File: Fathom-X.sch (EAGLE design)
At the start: 33 parts

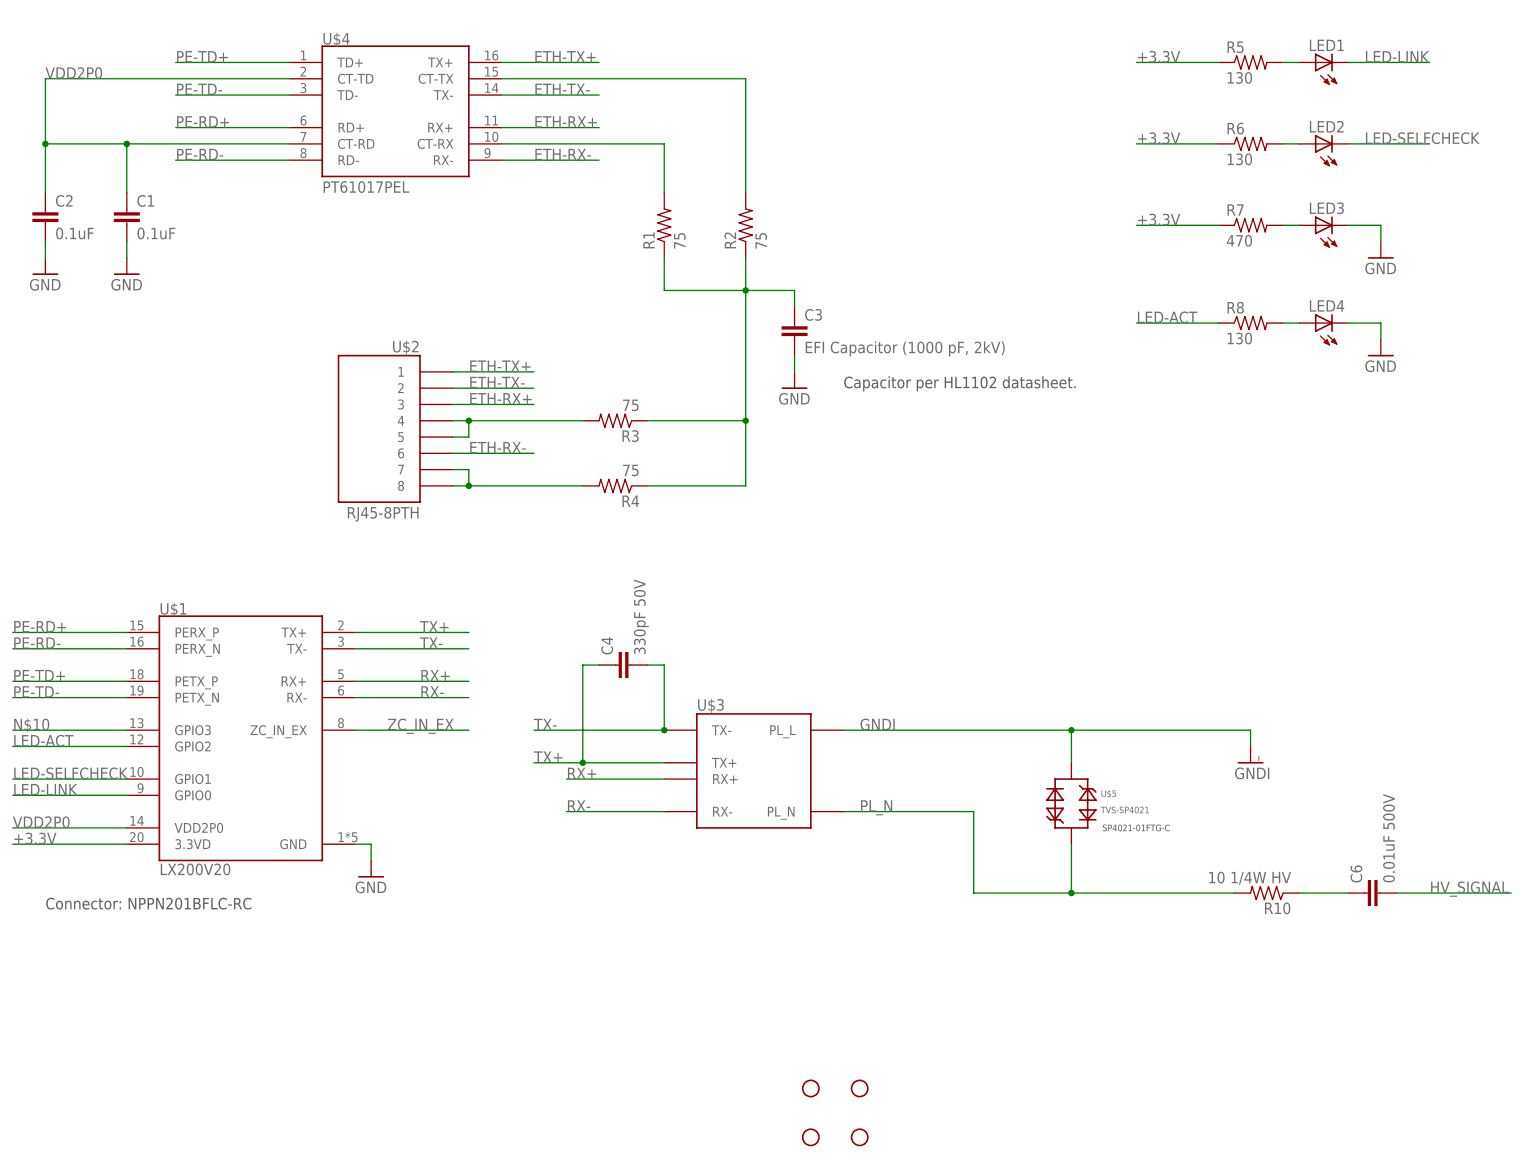
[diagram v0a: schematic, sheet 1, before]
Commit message: Divide to Fathom-E and Fathom-X. Both boards of this revision were ordered.
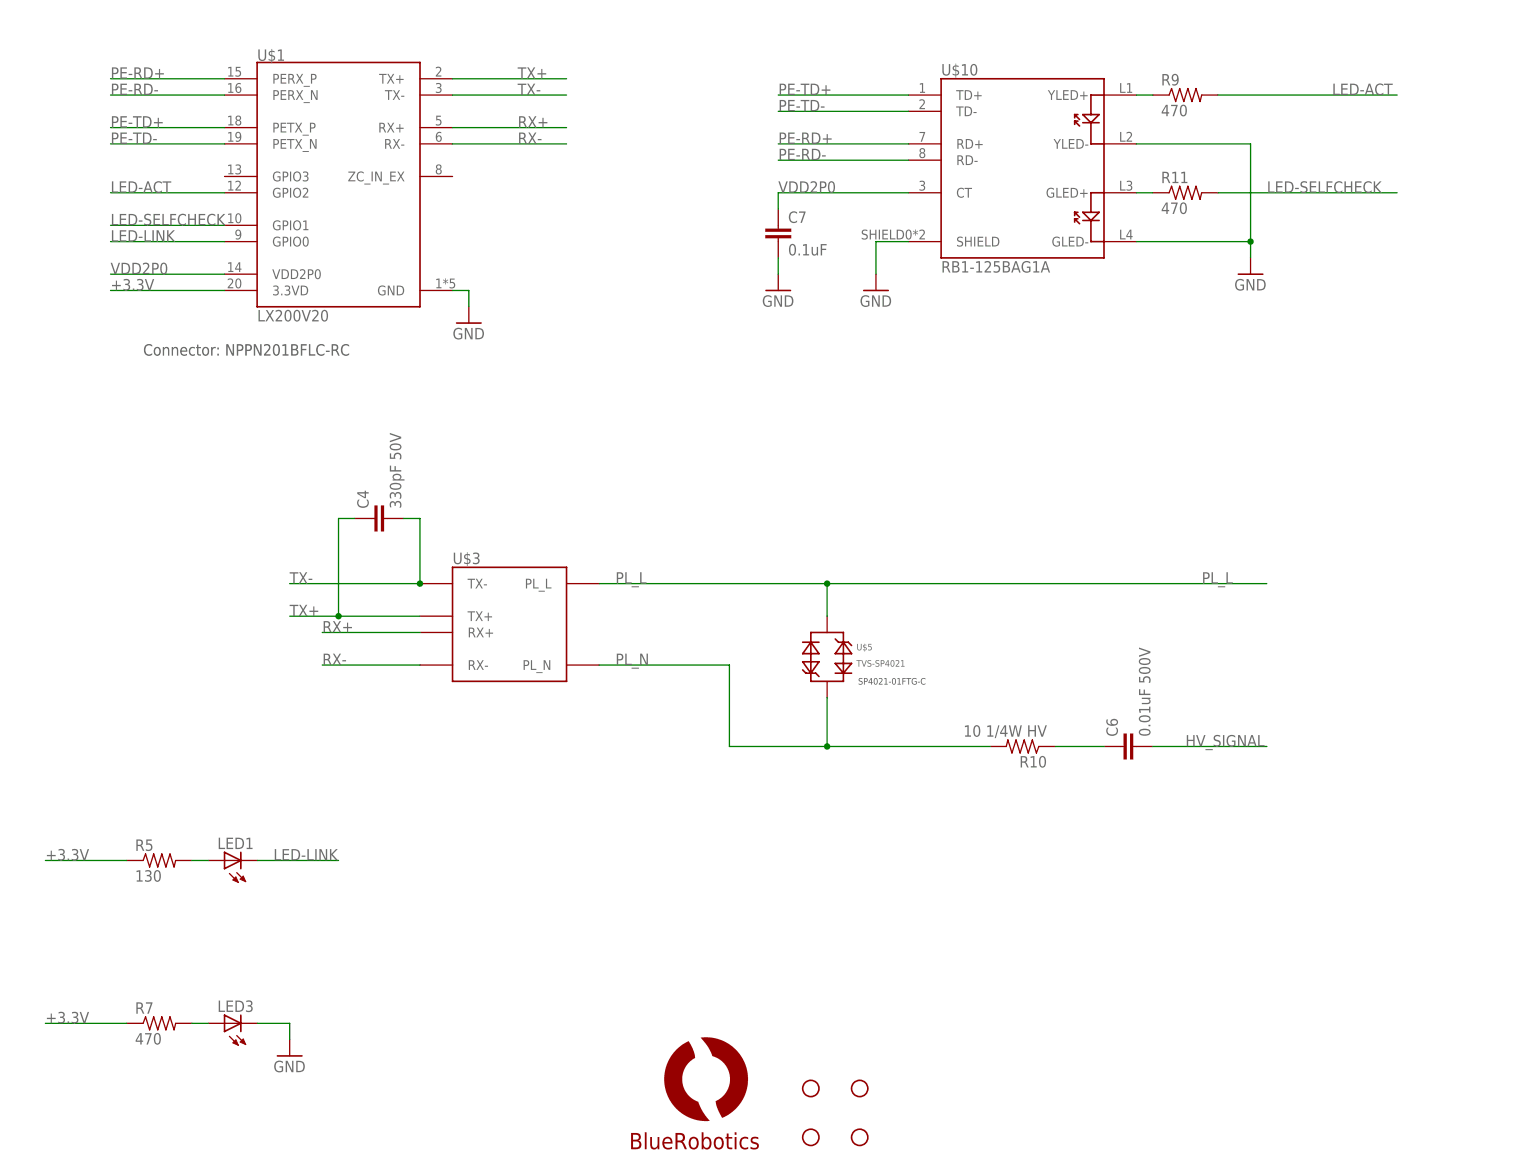
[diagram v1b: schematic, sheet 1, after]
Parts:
- removed C2: 0.1uF, resistor:C-EUC0402
- removed C3: EFI Capacitor (1000 pF, 2kV), resistor:C-EUC1206
- removed C5: 10uF, resistor:C-USC1206
- removed LED2, LED4: (no value), led:LEDCHIPLED_0603
- removed R1, R2, R3, R4: 75, resistor:R-US_R0603
- removed R6, R8: 130, resistor:R-US_R0603
- removed U$8: HEADER-2POWER, BlueRobotics-Main:HEADER-2POWER
- added C15: 0.1uF, SparkFun-Passives:CAP0603-CAP
- added C16: 10uF 10V, SparkFun-Passives:CAP_POL1206
- added C7: 0.1uF, resistor:C-EUC0603
- added D1: B340A, SparkFun-DiscreteSemi:DIODE-SCHOTTKY-B340A
- added IC1: 1117-3.3V, BlueRobotics-Main:VREG-1117-FIXEDSOT223
- added JP2: M023.5MM, SparkFun-Connectors:M023.5MM
- added JP3: USBSMD, SparkFun-Connectors:USBSMD
- added R11, R9: 470, resistor:R-US_R0603
- added U$10: RB1-125BAG1A, BlueRobotics-Main:RJ45-MAG
- C1: value 0.1uF -> 10uF 10V; device resistor:C-EUC0402 -> SparkFun-Passives:CAP_POL1206
- JP1: value (none) -> M02PTH; device SparkFun-Connectors:M083.5MM-8 -> SparkFun-Connectors:M02PTH
- U$2: value RJ45-8PTH -> HEADER-1NQ; device BlueRobotics-Main:RJ45-8PTH -> BlueRobotics-Main:HEADER-1NQ
- U$4: value PT61017PEL -> HEADER-1NQ; device BlueRobotics-Main:PT61017PEL -> BlueRobotics-Main:HEADER-1NQ
- U$6: value TETHER-HEADERSERIAL -> LOGOBR-LOGO-MS-COPPER; device BlueRobotics-Main:TETHER-HEADERSERIAL -> BlueRobotics-Main:LOGOBR-LOGO-MS-COPPER
- U$7: value HEADER-2POWER -> LOGOFULL-M; device BlueRobotics-Main:HEADER-2POWER -> BlueRobotics-Main:LOGOFULL-M
- U$9: value OKI-78SR-3.3V -> R-78E-0.5; device BlueRobotics-Main:VREG-OKI-78SR -> BlueRobotics-Main:VREG-R-78E-0.5
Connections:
- removed net 3.3V: C5.1, U$9.OUT
- removed net ETH-RX+: U$2.3, U$4.RX+
- removed net ETH-RX-: U$2.6, U$4.RX-
- removed net ETH-TX+: U$2.1, U$4.TX+
- removed net ETH-TX-: U$2.2, U$4.TX-
- removed net GNDI: JP1.3, U$3.PL_L, U$5.P$2
- removed net N$10: U$1.GPIO3
- removed net N$2: R2.2, U$4.CT-TX
- removed net N$3: R4.2, U$2.7, U$2.8
- removed net N$4: C3.1, R1.1, R2.1, R3.1, R4.1
- removed net N$5: R3.2, U$2.4, U$2.5
- removed net N$7: LED2.A, R6.2
- removed net N$9: LED4.A, R8.2
- removed net ZC_IN_EX: U$1.ZC_IN_EX
- new net 5V: C1.+, C15.1, D1.C, IC1.IN, U$9.OUT
- new net N$12: R9.1, U$10.YLED+
- new net N$13: R11.1, U$10.GLED+
- new net PL_L: JP1.2, U$3.PL_L, U$4.1, U$5.P$2
- net +3.3V: now also C16.+, IC1.OUT; no longer R6.1
- net GND: now also C1.-, C15.2, C16.-, C7.2, IC1.GND, JP2.1, JP3.GND, U$10.GLED-, U$10.SHIELD, U$10.YLED-; no longer C1.2, C2.2, C3.2, C5.2, LED4.C, U$7.1
- net HV_SIGNAL: now also U$2.1; no longer JP1.4
- net LED-ACT: now also R9.2; no longer R8.1
- net LED-SELFCHECK: now also R11.2; no longer LED2.C
- net N$1: now also D1.A, JP3.VBUS; no longer R1.2, U$4.CT-RX
- net PE-RD+: now also U$10.RD+; no longer U$4.RD+
- net PE-RD-: now also U$10.RD-; no longer U$4.RD-
- net PE-TD+: now also U$10.TD+; no longer U$4.TD+
- net PE-TD-: now also U$10.TD-; no longer U$4.TD-
- net PL_N: now also JP1.1
- net VDD2P0: now also C7.1, U$10.CT; no longer C1.1, C2.1, U$4.CT-RD, U$4.CT-TD
- net VIN: now also JP2.2; no longer U$7.2
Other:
- note removed: "Capacitor per HL1102 datasheet."
- moved on the sheet: C4, C6, LED1, LED3, R10, R5, R7, U$1, U$3, U$5, U$9

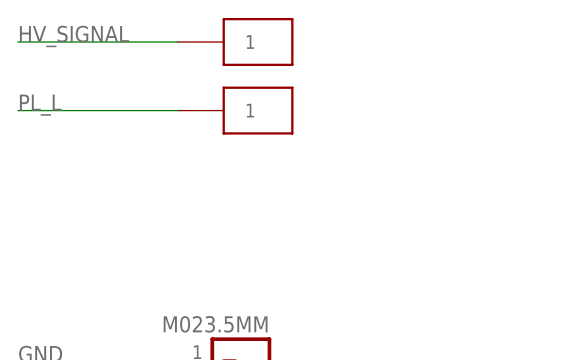
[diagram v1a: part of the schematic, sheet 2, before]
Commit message: Fathom-X: Update signal connector
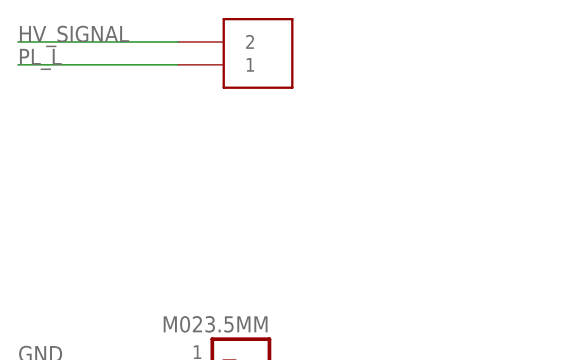
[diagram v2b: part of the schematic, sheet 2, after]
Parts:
- removed U$2, U$4: HEADER-1NQ, BlueRobotics-Main:HEADER-1NQ
- added U$8: HEADER-2POWER, BlueRobotics-Main:HEADER-2POWER
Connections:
- net HV_SIGNAL: now also U$8.2; no longer U$2.1
- net PL_L: now also U$8.1; no longer U$4.1
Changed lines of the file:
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@@
 <part name="R11" library="resistor" deviceset="R-US_" device="R0603" value="470"/>
 <part name="GND11" library="supply1" deviceset="GND" device=""/>
-<part name="U$2" library="BlueRobotics-Main" deviceset="HEADER-1" device="NQ"/>
-<part name="U$4" library="BlueRobotics-Main" deviceset="HEADER-1" device="NQ"/>
 <part name="JP2" library="SparkFun-Connectors" deviceset="M02" device="3.5MM"/>
 <part name="JP1" library="SparkFun-Connectors" deviceset="M02" device="PTH"/>
@@
 <part name="C1" library="SparkFun-Passives" deviceset="CAP_POL" device="1206" value="10uF 10V"/>
 <part name="IC1" library="BlueRobotics-Main" deviceset="VREG-1117-FIXED" device="SOT223" value="1117-3.3V"/>
+<part name="U$8" library="BlueRobotics-Main" deviceset="HEADER-2" device="POWER"/>
 </parts>
 <sheets>
@@
 <instance part="GND7" gate="1" x="111.76" y="81.28"/>
 <instance part="GND8" gate="1" x="134.62" y="81.28"/>
-<instance part="U$2" gate="G$1" x="60.96" y="137.16" rot="R180"/>
-<instance part="U$4" gate="G$1" x="60.96" y="129.54" rot="R180"/>
 <instance part="JP2" gate="G$1" x="55.88" y="99.06" rot="R180"/>
 <instance part="JP1" gate="G$1" x="55.88" y="81.28" rot="R180"/>
@@
 <instance part="D1" gate="G$1" x="147.32" y="114.3" rot="R180"/>
 <instance part="U$7" gate="G$1" x="124.46" y="10.16"/>
+<instance part="U$8" gate="G$1" x="60.96" y="137.16" rot="R180"/>
 </instances>
 <busses>
@@
 <wire x1="48.26" y1="134.62" x2="30.48" y2="134.62" width="0.1524" layer="91"/>
 <label x="30.48" y="134.62" size="1.778" layer="95"/>
-<pinref part="U$2" gate="G$1" pin="1"/>
+<pinref part="U$8" gate="G$1" pin="2"/>
 </segment>
 </net>
@@
 </segment>
 <segment>
-<wire x1="48.26" y1="127" x2="30.48" y2="127" width="0.1524" layer="91"/>
-<label x="30.48" y="127" size="1.778" layer="95"/>
-<pinref part="U$4" gate="G$1" pin="1"/>
-</segment>
-</net>
+<wire x1="48.26" y1="132.08" x2="30.48" y2="132.08" width="0.1524" layer="91"/>
+<label x="30.48" y="132.08" size="1.778" layer="95"/>
+<pinref part="U$8" gate="G$1" pin="1"/>
+</segment>
+</net>

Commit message: Change connector.
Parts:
- removed JP1: M02PTH, SparkFun-Connectors:M02PTH
- U$8: value HEADER-2POWER -> HEADER-210.16MM; device BlueRobotics-Main:HEADER-2POWER -> BlueRobotics-Main:HEADER-210.16MM
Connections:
- net PL_L: no longer JP1.2
- net PL_N: no longer JP1.1
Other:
- note added: "HomePlug/IEEE1901 Module"
- note added: "Jack with Magnetics"
- note added: "Powerline Coupling"
- moved on the sheet: C1, C15, C16, D1, IC1, JP2, U$9
